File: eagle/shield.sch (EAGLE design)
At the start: 41 parts, among them IC1 ATMEGA328P-AU, J1 22-27-2021-02, Q2 BSS138, Q3 BSS138, T1 BC517

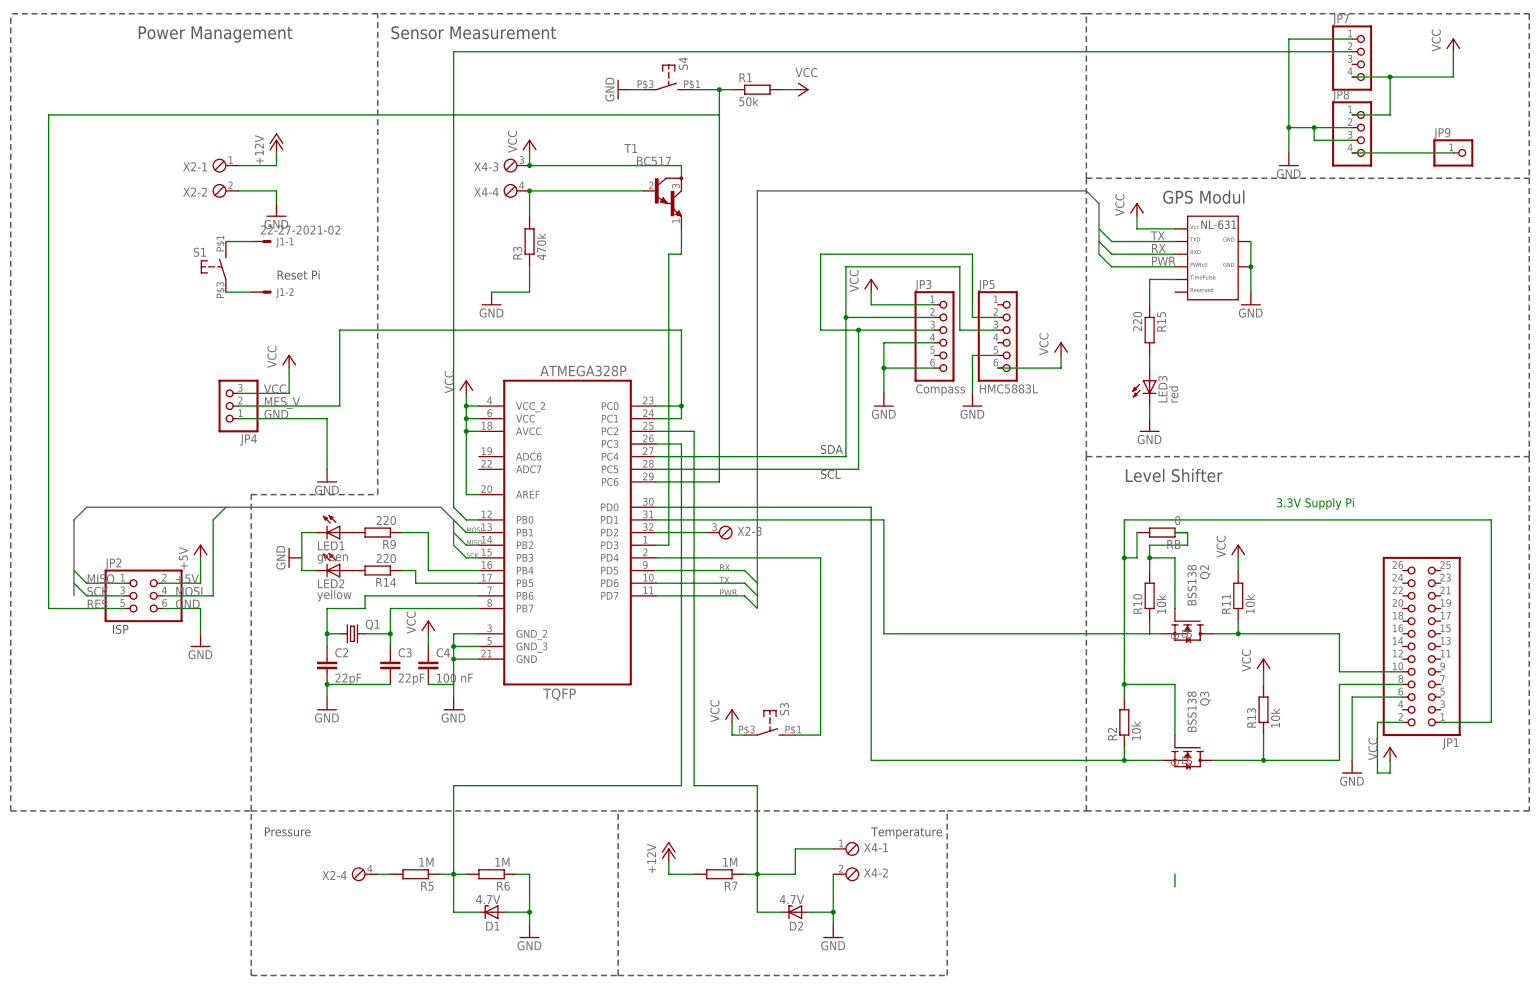
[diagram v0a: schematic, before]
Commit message: added breakout for navi on an extra board
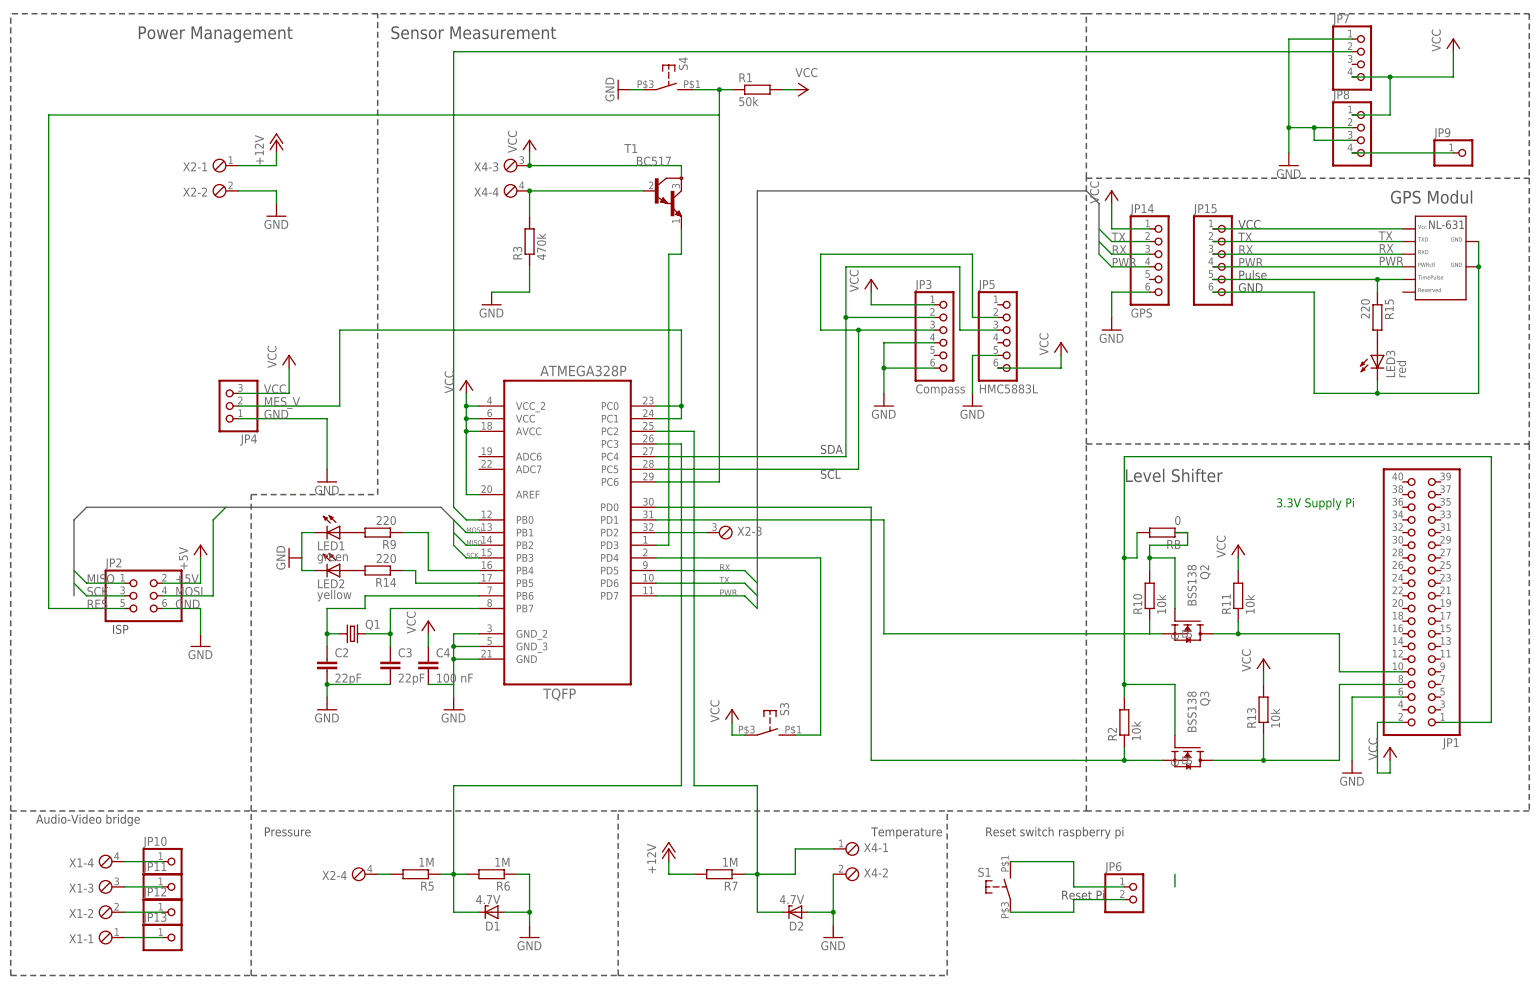
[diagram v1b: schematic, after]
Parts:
- removed J1: 22-27-2021-02, con-molex:22-27-2021-02
- added JP10, JP11, JP12, JP13: (no value), pinhead:PINHD-1X1
- added JP14: GPS, pinhead:PINHD-1X6
- added JP15: (no value), pinhead:PINHD-1X6
- added JP6: (no value), pinhead:PINHD-1X2
- added X1: (no value), con-phoenix-254:MPT4
- JP1: device pinhead:PINHD-2X13 -> pinhead:PINHD-2X20
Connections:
- new net N$13: JP10.1, X1-4.1
- new net N$14: JP11.1, X1-3.1
- new net N$15: JP12.1, X1-2.1
- new net N$16: JP13.1, X1-1.1
- new net N$17: JP15.1, U$2.P$1
- new net N$18: JP15.6, LED3.C, U$2.P$7, U$2.P$8
- net GND: now also JP14.6; no longer LED3.C, U$2.P$7, U$2.P$8
- net N$27: now also JP6.1; no longer J1-1.S
- net N$28: now also JP6.2; no longer J1-2.S
- net N$32: now also JP15.5
- net PWR: now also JP14.4, JP15.4
- net RX: now also JP14.3, JP15.3
- net TX: now also JP14.2, JP15.2
- net VCC: now also JP14.1; no longer U$2.P$1
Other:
- note added: "Audio-Video bridge"
- note added: "GND"
- note added: "Pulse"
- note added: "Reset switch raspberry pi"
- note added: "VCC"
- moved on the sheet: LED3, R15, S1

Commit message: first board design
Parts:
- removed R15: 220, resistor:R-EU_R1206
- removed RB: 0, resistor:R-EU_R1206
- removed U$2: NAVILOK-NL-631ETTL, 0liver:NAVILOK-NL-631ETTL
- added R4: 10k, resistor:R-EU_R1206
- JP15: device pinhead:PINHD-1X6 -> pinhead:PINHD-1X2
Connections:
- removed net N$18: JP15.6, LED3.C, U$2.P$7, U$2.P$8
- removed net N$32: JP15.5, R15.1, U$2.P$5
- removed net N$33: LED3.A, R15.2
- net GND: now also JP15.2, LED3.C
- net N$12: now also LED3.A, R4.2; no longer JP1.1, Q3.G, R2.2, RB.2
- net N$17: now also JP1.11, R4.1; no longer JP15.1, U$2.P$1
- net N$51: now also JP1.1, Q3.G, R2.2; no longer RB.1
- net PWR: no longer JP15.4, U$2.P$4
- net RX: no longer JP15.3, U$2.P$3
- net TX: no longer JP15.2, U$2.P$2
- net VCC: now also JP15.1
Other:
- note removed: "GND"
- note removed: "Pulse"
- note removed: "VCC"
- moved on the sheet: LED3
